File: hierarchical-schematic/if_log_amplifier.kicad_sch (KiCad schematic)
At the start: 58 parts, among them J6 Conn_Coaxial, U301 AD603AQ, U302 L78L05_TO92, U303 LM317L_TO92, U304 AD8307AN, U305 CA3140

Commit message: 2ndmixer-2ndlo
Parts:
- renumbered C812 to C325, C813 to C326, J6 to J301, R318 to R317, R319 to R318, R320 to R319, R321 to R320, R322 to R321, R323 to R322, R2 to R323, RV317 to RV301
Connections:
- net V+10 is gone; now on net +10: R310.2, R311.1
- net +15 renamed +15 Regulated

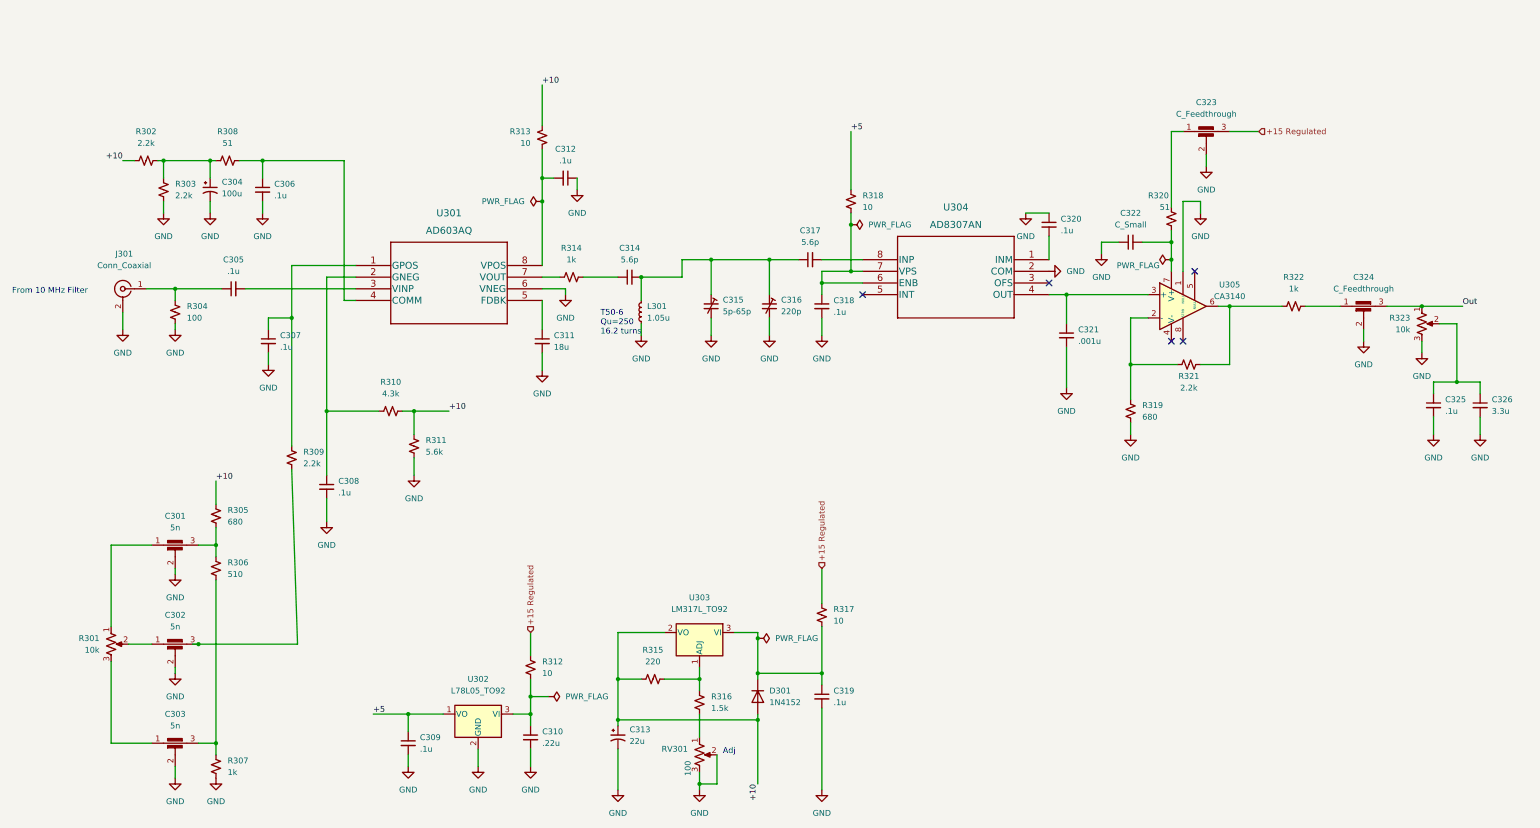
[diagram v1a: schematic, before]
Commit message: improved if and log amp and second lo/mixer
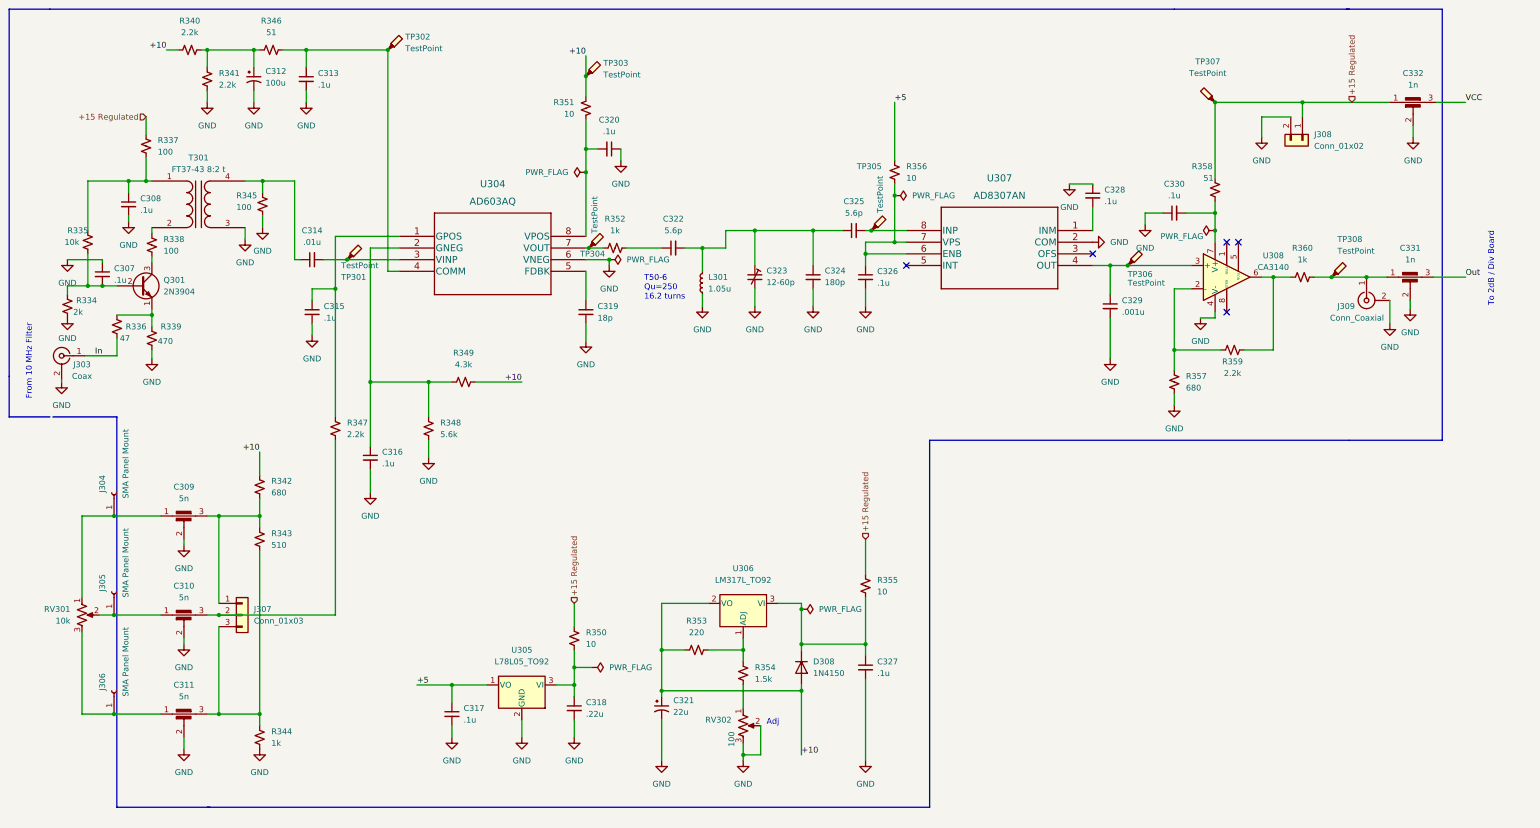
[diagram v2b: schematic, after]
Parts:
- removed C301, C302, C303: 5n, symbol Device:C_Feedthrough
- removed C304: 100u, symbol Device:C_Polarized_Small_US
- removed C305, C306, C309, C312: .1u, symbol Device:C_Small
- removed C310: .22u, symbol Device:C_Small
- removed C311: 18u, symbol Device:C_Small
- removed C313: 22u, symbol Device:C_Polarized_Small_US
- removed C315: 5p-65p, symbol Device:C_Trim_Small
- removed C316: 220p, symbol Device:C_Trim_Small
- removed C321: .001u, symbol Device:C_Small
- removed C323, C324: C_Feedthrough, symbol Device:C_Feedthrough
- removed D301: 1N4152, Diode_THT:D_DO-35_SOD27_P7.62mm_Horizontal, symbol Diode:1N4152
- removed J301: Conn_Coaxial, symbol Connector:Conn_Coaxial
- removed R301, R323: 10k, symbol Device:R_Potentiometer_US
- removed R302, R303, R309, R321: 2.2k, symbol Device:R_Small_US
- removed R304: 100, symbol Device:R_Small_US
- removed R305, R319: 680, symbol Device:R_Small_US
- removed R306: 510, symbol Device:R_Small_US
- removed R307, R314, R322: 1k, symbol Device:R_Small_US
- removed R308, R320: 51, symbol Device:R_Small_US
- removed R310: 4.3k, symbol Device:R_Small_US
- removed R311: 5.6k, symbol Device:R_Small_US
- removed R312, R313, R317, R318: 10, symbol Device:R_Small_US
- removed R315: 220, symbol Device:R_Small_US
- removed R316: 1.5k, symbol Device:R_Small_US
- removed U301: AD603AQ, Q_8_ADI, symbol AD630AQ:AD603AQ
- removed U302: L78L05_TO92, Package_TO_SOT_THT:TO-92_Inline, symbol Regulator_Linear:L78L05_TO92
- removed U303: LM317L_TO92, Package_TO_SOT_THT:TO-92_Inline, symbol Regulator_Linear:LM317L_TO92
- removed U304: AD8307AN, N_8_ADI, symbol AD8307AN:AD8307AN
- removed U305: CA3140, symbol Amplifier_Operational:CA3140
- added C309, C310, C311: 5n, if-log-amp:DSS1NB32A102Q91A, symbol Device:C_Feedthrough
- added C312: 100u, Capacitor_THT:CP_Radial_D5.0mm_P2.50mm, symbol Device:C_Polarized_Small_US
- added C313, C315, C316, C327, C328, C330: .1u, Capacitor_THT:C_Disc_D5.0mm_W2.5mm_P5.00mm, symbol Device:C_Small
- added C321: 22u, Capacitor_THT:CP_Radial_D5.0mm_P2.50mm, symbol Device:C_Polarized_Small_US
- added C323: 12-60p, if-log-amp:GKG60015, symbol Device:C_Trim_Small
- added C324: 180p, Capacitor_THT:C_Disc_D5.0mm_W2.5mm_P5.00mm, symbol Device:C_Small
- added C329: .001u, Capacitor_THT:CP_Radial_D5.0mm_P2.50mm, symbol Device:C_Small
- added C331, C332: 1n, if-log-amp:DSS1NB32A102Q91A, symbol Device:C_Feedthrough
- added D308: 1N4150, Diode_THT:D_DO-35_SOD27_P7.62mm_Horizontal, symbol Diode:1N4152
- added J303: Coax, Connector_Wire:SolderWire-0.5sqmm_1x02_P4.6mm_D0.9mm_OD2.1mm, symbol Connector:Conn_Coaxial
- added J304, J305, J306: SMA Panel Mount, symbol Connector:Conn_01x01_Female
- added J307: Conn_01x03, Connector_Wire:SolderWire-0.5sqmm_1x03_P4.6mm_D0.9mm_OD2.1mm, symbol Connector_Generic:Conn_01x03
- added J308: Conn_01x02, if-log-amp:691103110002, symbol Connector_Generic:Conn_01x02
- added J309: Conn_Coaxial, Connector_Wire:SolderWire-0.5sqmm_1x02_P4.6mm_D0.9mm_OD2.1mm, symbol Connector:Conn_Coaxial
- added Q301: 2N3904, Package_TO_SOT_THT:TO-92_Inline, symbol Transistor_BJT:2N3904
- added R334: 2k, Resistor_THT:R_Axial_DIN0207_L6.3mm_D2.5mm_P7.62mm_Horizontal, symbol Device:R_Small_US
- added R335: 10k, Resistor_THT:R_Axial_DIN0207_L6.3mm_D2.5mm_P7.62mm_Horizontal, symbol Device:R_Small_US
- added R336: 47, Resistor_THT:R_Axial_DIN0207_L6.3mm_D2.5mm_P7.62mm_Horizontal, symbol Device:R_Small_US
- added R337, R338, R345: 100, Resistor_THT:R_Axial_DIN0207_L6.3mm_D2.5mm_P7.62mm_Horizontal, symbol Device:R_Small_US
- added R339: 470, Resistor_THT:R_Axial_DIN0207_L6.3mm_D2.5mm_P7.62mm_Horizontal, symbol Device:R_Small_US
- added R340, R341, R347, R359: 2.2k, Resistor_THT:R_Axial_DIN0207_L6.3mm_D2.5mm_P7.62mm_Horizontal, symbol Device:R_Small_US
- added R342, R357: 680, Resistor_THT:R_Axial_DIN0207_L6.3mm_D2.5mm_P7.62mm_Horizontal, symbol Device:R_Small_US
- added R343: 510, Resistor_THT:R_Axial_DIN0207_L6.3mm_D2.5mm_P7.62mm_Horizontal, symbol Device:R_Small_US
- added R344, R352, R360: 1k, Resistor_THT:R_Axial_DIN0207_L6.3mm_D2.5mm_P7.62mm_Horizontal, symbol Device:R_Small_US
- added R346, R358: 51, Resistor_THT:R_Axial_DIN0207_L6.3mm_D2.5mm_P7.62mm_Horizontal, symbol Device:R_Small_US
- added R348: 5.6k, Resistor_THT:R_Axial_DIN0207_L6.3mm_D2.5mm_P7.62mm_Horizontal, symbol Device:R_Small_US
- added R349: 4.3k, Resistor_THT:R_Axial_DIN0207_L6.3mm_D2.5mm_P7.62mm_Horizontal, symbol Device:R_Small_US
- added R350, R351, R355, R356: 10, Resistor_THT:R_Axial_DIN0207_L6.3mm_D2.5mm_P7.62mm_Horizontal, symbol Device:R_Small_US
- added R353: 220, Resistor_THT:R_Axial_DIN0207_L6.3mm_D2.5mm_P7.62mm_Horizontal, symbol Device:R_Small_US
- added R354: 1.5k, Resistor_THT:R_Axial_DIN0207_L6.3mm_D2.5mm_P7.62mm_Horizontal, symbol Device:R_Small_US
- added RV302: 100, if-log-amp:Potentiometer_Bourns_3386G_Vertical, symbol Device:R_Potentiometer_US
- added T301: FT37-43 8:2 t, Transformer_THT:Transformer_Toroid_Horizontal_D14.0mm_Amidon-T50, symbol Device:Transformer_1P_1S
- added TP301, TP302, TP303, TP304, TP305, TP306, TP307, TP308: TestPoint, TestPoint:TestPoint_Pad_1.0x1.0mm, symbol Connector:TestPoint_Probe
- added U304: AD603AQ, if-log-amp:AD603AQ, symbol AD603AQ:AD603AQ
- added U305: L78L05_TO92, Package_TO_SOT_THT:TO-92_Inline, symbol Regulator_Linear:L78L05_TO92
- added U306: LM317L_TO92, Package_TO_SOT_THT:TO-92_Inline, symbol Regulator_Linear:LM317L_TO92
- added U307: AD8307AN, if-log-amp:AD8307AN, symbol AD8307AN:AD8307AN
- added U308: CA3140, if-log-amp:CA3140EZ, symbol Amplifier_Operational:CA3140
- C307, C308, C320: footprint (none) -> Capacitor_THT:C_Disc_D5.0mm_W2.5mm_P5.00mm
- C314: value 5.6p -> .01u; footprint (none) -> Capacitor_THT:C_Disc_D5.0mm_W2.5mm_P5.00mm
- C317: value 5.6p -> .1u; footprint (none) -> Capacitor_THT:C_Disc_D5.0mm_W2.5mm_P5.00mm
- C318: value .1u -> .22u; footprint (none) -> Capacitor_THT:C_Disc_D5.0mm_W2.5mm_P5.00mm
- C319: value .1u -> 18p; footprint (none) -> Capacitor_THT:C_Disc_D5.0mm_W2.5mm_P5.00mm
- C322: value C_Small -> 5.6p; footprint (none) -> Capacitor_THT:C_Disc_D5.0mm_W2.5mm_P5.00mm
- C325: value .1u -> 5.6p; footprint (none) -> Capacitor_THT:C_Disc_D5.0mm_W2.5mm_P5.00mm
- C326: value 3.3u -> .1u; footprint (none) -> Capacitor_THT:C_Disc_D5.0mm_W2.5mm_P5.00mm
- L301: footprint (none) -> Inductor_THT:L_Toroid_Vertical_L13.0mm_W6.5mm_P5.60mm
- RV301: value 100 -> 10k; Spice_Lib_File (none) -> if-log-amp-spice\Pot.lib; Spice_Model (none) -> pot_alps_a; Spice_Netlist_Enabled (none) -> Y; Spice_Primitive (none) -> X
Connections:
- net +10: now also C321.1, D308.2 (A), R340.1, R342.1, R349.2, R351.1, R353.1, TP303.1, U306.2 (VO)
- net +15 Regulated: now also C332.1, J308.1 (Pin_1), R337.1, R350.1, R355.1, R358.2, TP307.1
- net +5: now also C317.1, R356.1, U305.1 (VO)
- net GND: now also C307.1, C317.2, C309.2, C310.2, C311.2, C312.2, C313.2, C315.2, C316.2, C321.2, C323.2, C324.2, C327.2, C328.1, C329.2, C330.1, C331.2, C332.2, J303.2 (Ext), J308.2 (Pin_2), J309.2 (Ext), R334.2, R339.2, R341.2, R344.2, R345.2, R348.2, R357.2, RV302.2, RV302.3, T301.3 (SA), U304.6 (VNEG), U305.2 (GND), U307.2 (COM), U308.4 (V-); no longer C307.2, C322.1, C325.2, RV301.2, RV301.3
- net Out: now also C331.3
- net at C319.1: now also U304.5 (FDBK)
- net at RV301.1: now also C309.1, J304.1 (Pin_1)
- net at C325.1: now also C322.2, L301.2, C323.1, C324.1; no longer C326.1
- net at C308.1: now also R335.1, R337.2, T301.1 (AA)
- net at C320.2: now also R351.2, U304.8 (VPOS)
- net at C314.1: now also R345.1, T301.4 (SB)
- net at C318.1: now also R350.2, U305.3 (VI)
- new net: C313.1, R346.2, TP302.1, U304.4 (COMM)
- new net: C314.2, TP301.1, U304.3 (VINP)
- new net: R359.1, R360.1, U308.6
- new net: R357.1, R359.2, U308.2 (-)
- new net: C315.1, R347.1, U304.1 (GPOS)
- new net: C310.3, J307.2 (Pin_2), R347.2
- new net: C309.3, J307.1 (Pin_1), R342.2, R343.1
- new net: C312.1, R340.2, R341.1, R346.1
- new net: C310.1, J305.1 (Pin_1), RV301.2
- new net: C311.1, J306.1 (Pin_1), RV301.3
- new net: Q301.1 (E), R336.1, R339.1
- new net: C307.2, Q301.2 (B), R334.1, R335.2
- new net: Q301.3 (C), R338.2
- new net: C330.2, R358.1, U308.7 (V+)
- new net: C327.1, D308.1 (K), R355.2, U306.3 (VI)
- new net: C329.1, TP306.1, U307.4 (OUT), U308.3 (+)
- new net: R354.2, RV302.1
- new net: C325.2, TP305.1, U307.8 (INP)
- new net: R338.1, T301.2 (AB)
- new net: C322.1, R352.2
- new net: C316.1, R348.1, R349.1, U304.2 (GNEG)
- new net: C311.3, J307.3 (Pin_3), R343.2, R344.1
- new net: R352.1, TP304.1, U304.7 (VOUT)
- new net: C331.1, J309.1 (In), R360.2, TP308.1
- new net: C328.2, U307.1 (INM)
- new net: C326.1, R356.2, U307.6 (ENB), U307.7 (VPS)
- new net: R353.2, R354.1, U306.1 (ADJ)
- new net In: J303.1 (In), R336.2
- new net VCC: C332.3
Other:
- note added: "To 2dB / Div Board"

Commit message: Hierarchical schematic updates
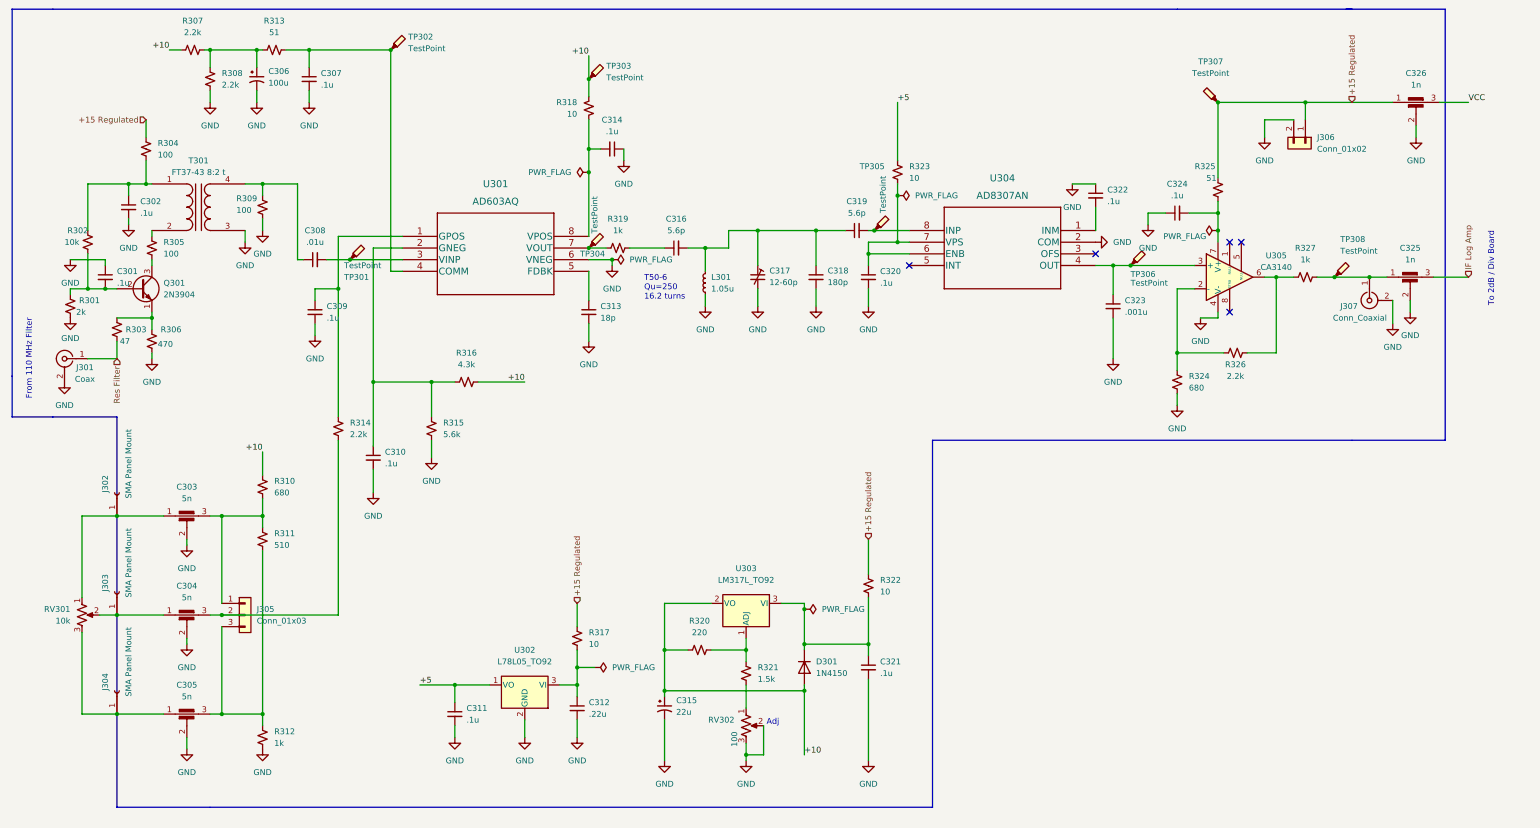
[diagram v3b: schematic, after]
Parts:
- renumbered C307 to C301, C308 to C302, C309 to C303, C310 to C304, C311 to C305, C312 to C306, C313 to C307, C314 to C308, C315 to C309, C316 to C310, C317 to C311, C318 to C312, C319 to C313, C320 to C314, C321 to C315, C322 to C316, C323 to C317, C324 to C318, C325 to C319, C326 to C320, C327 to C321, C328 to C322, C329 to C323, C330 to C324, C331 to C325, C332 to C326, D308 to D301, J303 to J301, J304 to J302, J305 to J303, J306 to J304, J307 to J305, J308 to J306, J309 to J307, R334 to R301, R335 to R302, R336 to R303, R337 to R304, R338 to R305, R339 to R306, R340 to R307, R341 to R308, R345 to R309, R342 to R310, R343 to R311, R344 to R312, R346 to R313, R347 to R314, R348 to R315, R349 to R316, R350 to R317, R351 to R318, R352 to R319, R353 to R320, R354 to R321, R355 to R322, R356 to R323, R357 to R324, R358 to R325, R359 to R326, R360 to R327, U304 to U301, U305 to U302, U306 to U303, U307 to U304, U308 to U305
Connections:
- net In renamed Res Filter
- net Out renamed IF Log Amp
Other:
- note added: "From 110 MHz Filter"
- note removed: "From 10 MHz Filter"
- moved on the sheet: C301, C302, C303, C304, C305, C306, C307, C308, C309, C310, C311, C312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

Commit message: hierarchical schematic updated to pass erc
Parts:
- U301: footprint if-log-amp:AD603AQ -> Q_8_ADI; symbol AD603AQ:AD603AQ -> spectrum analyzer:AD603AQ
- U304: footprint if-log-amp:AD8307AN -> N_8_ADI; symbol AD8307AN:AD8307AN -> spectrum analyzer:AD8307AN
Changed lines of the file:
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@@
   (junction (at 157.48 162.56) (diameter 0) (color 0 0 0 0)
-  )
-  (junction (at 146.05 68.58) (diameter 0) (color 0 0 0 0)
   )
   (junction (at 35.56 74.93) (diameter 0) (color 0 0 0 0)
@@
     (pin "1")
   )
-  (symbol (lib_id "power:PWR_FLAG") (at 146.05 68.58 270) (unit 1)
-    (in_bom yes) (on_board yes) (fields_autoplaced)
-    (property "Reference" "#FLG0303" (id 0) (at 147.955 68.58 0)
-      (effects (font (size 1.27 1.27)) hide)
-    )
-    (property "Value" "PWR_FLAG" (id 1) (at 149.86 68.5799 90)
-      (effects (font (size 1.27 1.27)) (justify left))
-    )
-    (property "Footprint" "" (id 2) (at 146.05 68.58 0)
-      (effects (font (size 1.27 1.27)) hide)
-    )
-    (property "Datasheet" "~" (id 3) (at 146.05 68.58 0)
-      (effects (font (size 1.27 1.27)) hide)
-    )
-    (pin "1")
-  )
   (symbol (lib_id "power:GND") (at 93.98 119.38 0) (unit 1)
     (in_bom yes) (on_board yes) (fields_autoplaced)
@@
     (pin "2")
   )
-  (symbol (lib_id "AD8307AN:AD8307AN") (at 251.46 62.23 0) (mirror y) (unit 1)
+  (symbol (lib_id "spectrum analyzer:AD8307AN") (at 251.46 62.23 0) (mirror y) (unit 1)
     (in_bom yes) (on_board yes) (fields_autoplaced)
     (property "Reference" "U304" (id 0) (at 231.14 50.8 0)
@@
       (effects (font (size 1.524 1.524)))
     )
-    (property "Footprint" "if-log-amp:AD8307AN" (id 2) (at 231.14 56.134 0)
+    (property "Footprint" "N_8_ADI" (id 2) (at 231.14 56.134 0)
       (effects (font (size 1.524 1.524)) hide)
     )
@@
       (effects (font (size 1.27 1.27)) hide)
     )
-    (property "Datasheet" "https://www.renesas.com/us/en/document/dst/ca3140-ca3140a-datasheet" (id 3) (at 280.67 72.39 0)
+    (property "Datasheet" "http://www.intersil.com/content/dam/intersil/documents/ca31/ca3140-a.pdf" (id 3) (at 280.67 72.39 0)
       (effects (font (size 1.27 1.27)) hide)
     )
@@
     (pin "1")
   )
-  (symbol (lib_id "AD603AQ:AD603AQ") (at 100.33 63.5 0) (unit 1)
+  (symbol (lib_id "spectrum analyzer:AD603AQ") (at 100.33 63.5 0) (unit 1)
     (in_bom yes) (on_board yes) (fields_autoplaced)
     (property "Reference" "U301" (id 0) (at 120.65 52.07 0)
@@
       (effects (font (size 1.524 1.524)))
     )
-    (property "Footprint" "if-log-amp:AD603AQ" (id 2) (at 120.65 57.404 0)
+    (property "Footprint" "Q_8_ADI" (id 2) (at 120.65 57.404 0)
       (effects (font (size 1.524 1.524)) hide)
     )

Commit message: v7 conversion
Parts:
- D301: Spice_Lib_File if-log-amp-spice\fairch.lib -> (none); Spice_Model 1N4152 -> (none); Spice_Netlist_Enabled Y -> (none); Spice_Node_Sequence 2 1 -> (none); Spice_Primitive D -> (none)
- J301, J307: Spice_Model Conn_Coaxial -> (none); Spice_Netlist_Enabled N -> (none); Spice_Primitive J -> (none)
- J302, J303, J304: Spice_Model SMA Panel Mount -> (none); Spice_Netlist_Enabled N -> (none); Spice_Primitive J -> (none)
- RV301: Spice_Lib_File if-log-amp-spice\Pot.lib -> (none); Spice_Model pot_alps_a -> (none); Spice_Netlist_Enabled Y -> (none); Spice_Primitive X -> (none)
- RV302: Spice_Lib_File if-log-amp-spice\Pot2.lib -> (none); Spice_Model pot_lin2 -> (none); Spice_Netlist_Enabled Y -> (none); Spice_Primitive X -> (none)
- TP301, TP302, TP303, TP304, TP305, TP306, TP307: value TestPoint -> ${SIM.PARAMS}; Spice_Netlist_Enabled N -> (none)
- TP308: value TestPoint -> ${SIM.PARAMS}; Spice_Netlist_Enabled N -> (none); Spice_Primitive R -> (none)
- U301: Spice_Lib_File if-log-amp-spice\ad603a.cir -> (none); Spice_Model AD603A -> (none); Spice_Netlist_Enabled Y -> (none); Spice_Primitive X -> (none)
- U302: Spice_Lib_File if-log-amp-spice\78L05_TEST.sub -> (none); Spice_Model X78L05 -> (none); Spice_Netlist_Enabled Y -> (none); Spice_Node_Sequence 3 2 1 -> (none); Spice_Primitive X -> (none)
- U303: Spice_Lib_File if-log-amp-spice\lm317.lib -> (none); Spice_Model LM317TI -> (none); Spice_Netlist_Enabled Y -> (none); Spice_Node_Sequence 3 1 2 -> (none); Spice_Primitive X -> (none)
- U304: value AD8307AN -> ${SIM.PARAMS}; Spice_Netlist_Enabled N -> (none); Spice_Primitive R -> (none)
- U305: Spice_Lib_File if-log-amp-spice\ca3140.sub -> (none); Spice_Model ca3140 -> (none); Spice_Netlist_Enabled Y -> (none); Spice_Primitive X -> (none)
